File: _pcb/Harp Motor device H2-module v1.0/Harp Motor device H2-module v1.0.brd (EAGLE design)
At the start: 43 x 57.4 mm, 67 parts, among them IC1 FT232RL, IC2 74LVC1G07DBV, IC3 LP5907MFX-3.3, IC4 74LVC1G07DBV, IC5 74LVC1G07DBV, IC6 74LVC1G07DBV, IC7 USBLC6-2SC6, IC8 ATXMEGA32A4U, T1 DMG1012UW, T2 DMG1012UW, X1 2x5 header, X15 Main_plug, X2 2x5 header, X3 USB_MINI_B

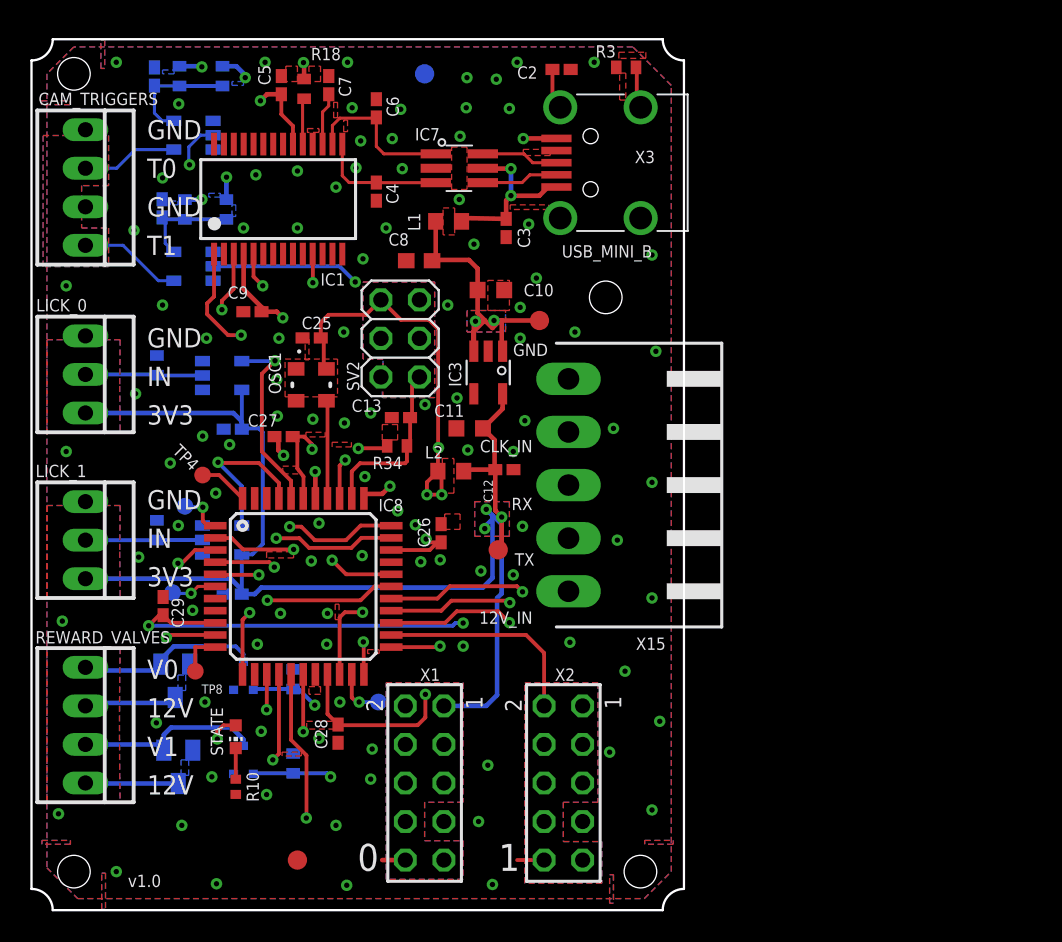
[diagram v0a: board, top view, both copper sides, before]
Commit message: BOMs & start Harp Motor device H2-module v1.0
. almost final BOMs versions for VestibularVR H1-module v1.0 & Lick Sensor module v1.0
. start of new project Harp Motor device H2-module v1.0
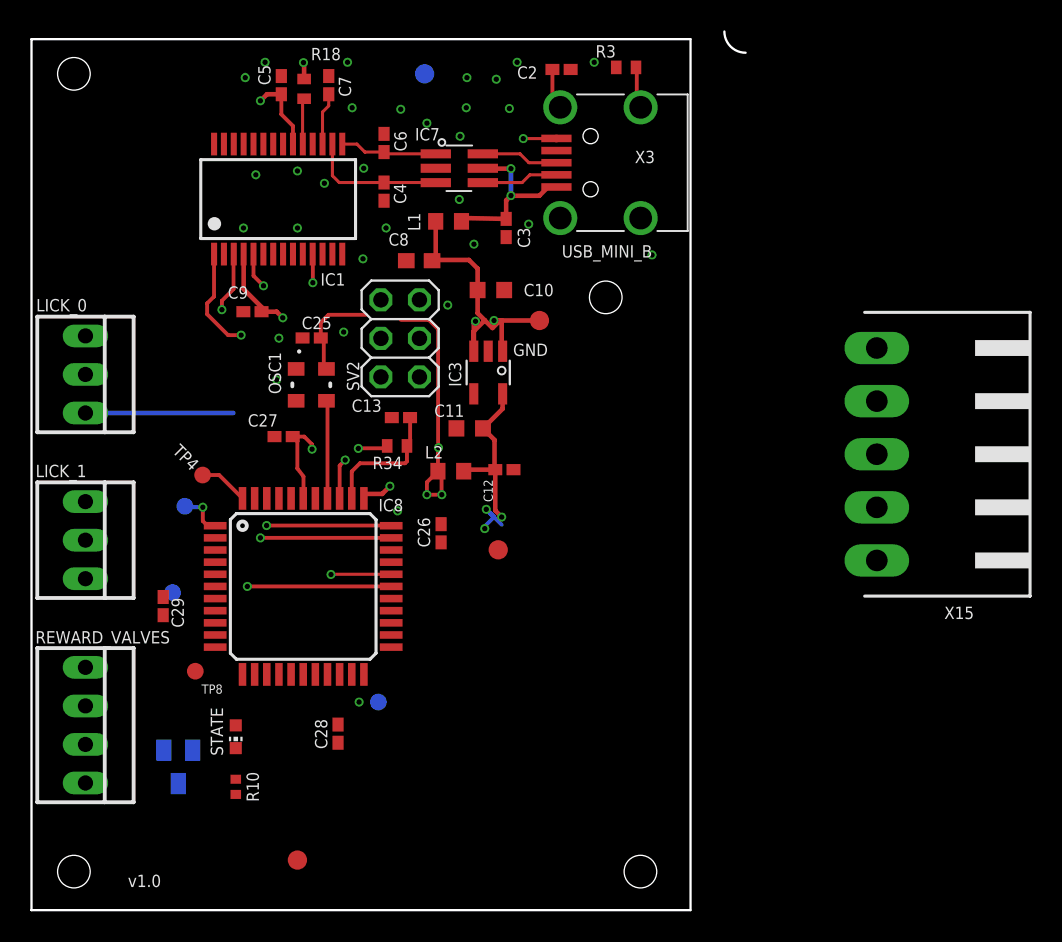
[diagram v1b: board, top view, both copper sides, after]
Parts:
- removed C14, C15, C16, C17: 100nF, rcl:C0402K
- removed CAM_TRIGGERS: 1x4 case, con-molex:22-23-2041
- removed D1: BAT54, diode:SOT23
- removed IC2, IC4, IC5, IC6: 74LVC1G07DBV, VestibularVR H1-module v1.0:SOT23-5
- removed R1, R5: 0R, rcl:R0402@1
- removed R2, R6: DNI, rcl:R0402@1
- removed R4, R7: 10k, rcl:R0402@1
- removed R8, R9: 1M, rcl:R0402@1
- removed T1, T2: DMG1012UW, VestibularVR H1-module v1.0:SOT323
- removed X1, X2: 2x5 header, con-samtec:TSW-105-02-S-D
- LICK_0, LICK_1: value 2x3 case -> 1x3 case
- REWARD_VALVES: value 22-23-2041 -> 1x4 case
- moved X15 20.4 mm to (61.0, 30.0)
- moved C6 2.34 mm to (23.2, 50.6)
- moved C4 0.51 mm to (23.2, 47.4)
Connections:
- removed net LICK_PORT_1: IC6.2, LICK_0.2, R9.2
- removed net LICK_PORT_2: IC5.2, LICK_1.2, R8.2
- removed net N$14: C15.1, IC2.5, R5.2, R6.2
- removed net N$4: CAM_TRIGGERS.4, IC2.4
- removed net N$5: C16.1, IC4.5, R1.2, R2.2
- removed net N$68: D1.1, REWARD_VALVES.1, T2.3
- removed net N$8: CAM_TRIGGERS.2, IC4.4
- removed net U_CAM1_TRIGGER: IC4.2, IC8.10
- removed net U_CAM2_TRIGGER: IC2.2, IC8.20
- removed net U_LICK_PORT_1: IC6.4, IC8.40
- removed net U_LICK_PORT_2: IC5.4, IC8.41
- removed net U_OPTICAL_FLOW_1_CS: IC8.14, X1.2
- removed net U_OPTICAL_FLOW_1_INT: IC8.4, X1.6
- removed net U_OPTICAL_FLOW_1_MISO: IC8.16, X1.5
- removed net U_OPTICAL_FLOW_1_MOSI: IC8.15, X1.4
- removed net U_OPTICAL_FLOW_1_SCK: IC8.17, X1.3
- removed net U_OPTICAL_FLOW_2_CS: IC8.24, X2.2
- removed net U_OPTICAL_FLOW_2_INT: IC8.5, X2.6
- removed net U_OPTICAL_FLOW_2_MISO: IC8.26, X2.5
- removed net U_OPTICAL_FLOW_2_MOSI: IC8.25, X2.4
- removed net U_OPTICAL_FLOW_2_SCK: IC8.27, X2.3
- removed net U_REWARD_VALVE_1: IC8.2, R4.2, T2.1
- removed net U_REWARD_VALVE_2: IC8.3, R7.2, T1.1
- net +12V: no longer D1.3, REWARD_VALVES.2, REWARD_VALVES.4
- net +3V3: no longer C14.1, C17.1, IC5.5, IC6.5, R1.1, R5.1, X1.1, X2.1
- net +3V3_U: now also SV2.2; no longer SV2.6
- net +5V: no longer R2.1, R6.1
- net GND: now also SV2.6; no longer C14.2, C15.2, C16.2, C17.2, CAM_TRIGGERS.1, CAM_TRIGGERS.3, IC2.3, IC4.3, IC5.3, IC6.3, R4.1, R7.1, R8.1, R9.1, SV2.2, T1.2, T2.2, X1.10, X1.7, X2.10, X2.7
- net HARP_H1_BOARD_RX: no longer IC8.22
- net HARP_H1_BOARD_TX: no longer IC8.23
- net HARP_H1_CLOCK_IN: no longer IC8.12
- net N$6: no longer REWARD_VALVES.3, T1.3
- net PDI_CLK: now also SV2.5; no longer SV2.1
- net PDI_DATA: now also SV2.1; no longer SV2.5
- net USBDM: now also C4.1, IC7.P$3; no longer C6.1, IC7.P$1
- net USBDP: now also C6.1, IC7.P$1; no longer C4.1, IC7.P$3
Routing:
- net +3V3: track 200.1 -> 95.2 mm, vias 9 -> 7
- net +12V: track 90.7 -> 0.00 mm
- net +3V3_U: track 108.3 -> 41.6 mm, vias 9 -> 5
- net HARP_H1_CLOCK_IN: track 38.6 -> 0.00 mm, vias 2 -> 0
- net U_CAM1_TRIGGER: track 38.3 -> 0.00 mm, vias 2 -> 0
- net U_CAM2_TRIGGER: track 38.0 -> 0.00 mm, vias 2 -> 0
- net U_OPTICAL_FLOW_2_INT: track 36.7 -> 0.00 mm, vias 2 -> 0
- net U_OPTICAL_FLOW_1_INT: track 35.6 -> 0.00 mm, vias 2 -> 0
- net LED_STATE: track 34.9 -> 2.72 mm, vias 3 -> 1
- net U_REWARD_VALVE_2: track 30.8 -> 0.00 mm, vias 3 -> 0
- net U_OPTICAL_FLOW_2_MISO: track 24.5 -> 0.00 mm, vias 1 -> 0
- net U_OPTICAL_FLOW_2_SCK: track 22.0 -> 0.00 mm, vias 1 -> 0
- net U_REWARD_VALVE_1: track 21.4 -> 0.00 mm, vias 2 -> 0
- net U_OPTICAL_FLOW_1_MISO: track 19.9 -> 0.00 mm, vias 1 -> 0
- net U_OPTICAL_FLOW_2_MOSI: track 18.3 -> 0.00 mm, vias 1 -> 0
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- removed copper zone on layer 1, net +3V3
- removed copper zone on layer 15, net +3V3
- removed copper zone on layer 16, net +3V3
- removed copper zone on layer 2, net +3V3
- removed copper zone on layer 1, net +5V
- removed copper zone on layer 15, net +5V
- removed copper zone on layer 16, net +5V
- removed copper zone on layer 2, net +5V
- removed copper zone on layer 1, net 1
- removed copper zone on layer 1, net 123
- removed copper zone on layer 1, net GND
- removed copper zone on layer 15, net GND
- removed copper zone on layer 16, net GND
- removed copper zone on layer 2, net GND
- removed copper zone on layer 1, net N$10
- removed copper zone on layer 15, net N$100
- removed copper zone on layer 1, net N$101
- removed copper zone on layer 2, net N$102
- removed copper zone on layer 1, net N$106
- removed copper zone on layer 1, net N$107
- removed copper zone on layer 1, net N$108
- removed copper zone on layer 15, net N$109
- removed copper zone on layer 15, net N$110
- removed copper zone on layer 15, net N$111
- removed copper zone on layer 1, net N$16
- removed copper zone on layer 2, net N$19
- removed copper zone on layer 16, net N$20
- removed copper zone on layer 1, net N$21
- removed copper zone on layer 15, net N$22
- removed copper zone on layer 16, net N$23
- removed copper zone on layer 1, net N$24
- removed copper zone on layer 1, net N$25
- removed copper zone on layer 1, net N$26
- removed copper zone on layer 1, net N$27
- removed copper zone on layer 2, net N$28
- removed copper zone on layer 1, net N$29
- removed copper zone on layer 15, net N$30
- removed copper zone on layer 16, net N$31
- removed copper zone on layer 2, net N$32
- removed copper zone on layer 1, net N$33
- removed copper zone on layer 15, net N$34
- removed copper zone on layer 16, net N$35
- removed copper zone on layer 2, net N$36
- removed copper zone on layer 1, net N$37
- removed copper zone on layer 15, net N$39
- removed copper zone on layer 16, net N$40
- removed copper zone on layer 2, net N$41
- removed copper zone on layer 1, net N$42
- removed copper zone on layer 15, net N$43
- removed copper zone on layer 16, net N$44
- removed copper zone on layer 1, net N$45
- removed copper zone on layer 1, net N$46
- removed copper zone on layer 1, net N$47
- removed copper zone on layer 1, net N$48
- removed copper zone on layer 2, net N$49
- removed copper zone on layer 1, net N$50
- removed copper zone on layer 15, net N$51
- removed copper zone on layer 16, net N$52
- removed copper zone on layer 16, net N$53
- removed copper zone on layer 1, net N$54
- removed copper zone on layer 1, net N$55
- removed copper zone on layer 1, net N$56
- removed copper zone on layer 1, net N$57
- removed copper zone on layer 2, net N$58
- removed copper zone on layer 1, net N$59
- removed copper zone on layer 1, net N$60
- removed copper zone on layer 15, net N$61
- removed copper zone on layer 16, net N$62
- removed copper zone on layer 16, net N$63
- removed copper zone on layer 16, net N$64
- removed copper zone on layer 16, net N$65
- removed copper zone on layer 16, net N$66
- removed copper zone on layer 16, net N$67
- removed copper zone on layer 1, net N$69
- removed copper zone on layer 1, net N$7
- removed copper zone on layer 1, net N$70
- removed copper zone on layer 1, net N$71
- removed copper zone on layer 2, net N$72
- removed copper zone on layer 15, net N$73
- removed copper zone on layer 16, net N$74
- removed copper zone on layer 1, net N$75
- removed copper zone on layer 1, net N$76
- removed copper zone on layer 1, net N$77
- removed copper zone on layer 15, net N$78
- removed copper zone on layer 2, net N$79
- removed copper zone on layer 15, net N$80
- removed copper zone on layer 16, net N$81
- removed copper zone on layer 1, net N$82
- removed copper zone on layer 2, net N$83
- removed copper zone on layer 15, net N$84
- removed copper zone on layer 16, net N$85
- removed copper zone on layer 1, net N$86
- removed copper zone on layer 2, net N$87
- removed copper zone on layer 15, net N$88
- removed copper zone on layer 16, net N$89
- removed copper zone on layer 1, net N$90
- removed copper zone on layer 2, net N$91
- removed copper zone on layer 15, net N$92
- removed copper zone on layer 16, net N$93
- removed copper zone on layer 1, net N$94
- removed copper zone on layer 2, net N$95
- removed copper zone on layer 15, net N$96
- removed copper zone on layer 16, net N$97
- removed copper zone on layer 15, net N$98
- removed copper zone on layer 15, net N$99
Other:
- board size 43 x 57.4 mm -> 47.1 x 57.9 mm
- board text removed: "0"
- board text removed: "1"
- board text removed: "12V"
- board text removed: "12V_IN"
- board text removed: "3V3"
- board text removed: "CLK_IN"
- board text removed: "IN"
- board text removed: "RX"
- board text removed: "T0"
- board text removed: "T1"
- board text removed: "TX"
- board text removed: "V0"
- board text removed: "V1"
